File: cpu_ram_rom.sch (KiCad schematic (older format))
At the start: 14 parts, among them U12 74HCT3G04, U4 Z84C0010AEG, U5 IS62C5128BL-45TLI, U6 SST39SF040

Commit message: layout changes, silkscreen fixes
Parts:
- removed D13, D14: Green, LED_SMD:LED_0603_1608Metric_Pad1.05x0.95mm_HandSolder, symbol Device:LED
- removed R40, R41: 360R, Resistor_SMD:R_0603_1608Metric_Pad1.05x0.95mm_HandSolder, symbol Device:R_Small
- removed U12: 74HCT3G04, Package_SO:TSSOP-8_3x3mm_P0.65mm, symbol THS-80-rescue:74HCT3G04-74xGxx
- added D2, D3: GRN, LED_SMD:LED_0603_1608Metric_Pad1.05x0.95mm_HandSolder, symbol Device:LED
- added D4: RED, LED_SMD:LED_0603_1608Metric_Pad1.05x0.95mm_HandSolder, symbol Device:LED
- added R10, R11: 1K, Resistor_SMD:R_0603_1608Metric_Pad1.05x0.95mm_HandSolder, symbol Device:R_Small
- added R12: 360R, Resistor_SMD:R_0603_1608Metric_Pad1.05x0.95mm_HandSolder, symbol Device:R_Small
- added U5: 74LVC2G02, Package_SO:TSSOP-8_3x3mm_P0.65mm, symbol 74xGxx:74LVC2G02
- renumbered C18 to C10, C16 to C8, C17 to C9, R19 to R7, R21 to R8, R20 to R9, U5 to U3, U6 to U4, U4 to U6
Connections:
- net labels added: VCC
- net labels removed: +5V
- wire segments 117 -> 118
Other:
- note added: "RAM Enabled"
- note added: "ROM Enabled"
- note added: "ROM Write Enabled"

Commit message: started routing
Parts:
- removed U3: IS62C5128BL-45TLI, Package_SO:TSOP-II-32_21.0x10.2mm_P1.27mm, symbol THS-80:IS62C5128BL-45TLI
- added U3: AS6C4008A-55ZIN, Package_SO:TSOP-II-32_21.0x10.2mm_P1.27mm, symbol Memory_RAM:AS6C4008A-55ZIN
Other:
- moved on the sheet: R7, R8, R9, U4

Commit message: changes
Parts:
- U3: symbol Memory_RAM:AS6C4008A-55ZIN -> THS-80-rescue:AS6C4008A-55ZIN-Memory_RAM
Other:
- moved on the sheet: U6

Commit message: cleaned up
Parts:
- removed U5: 74LVC2G02, Package_SO:TSSOP-8_3x3mm_P0.65mm, symbol 74xGxx:74LVC2G02
- added U14: 74AHCT2G04, Package_TO_SOT_SMD:SOT-363_SC-70-6_Handsoldering, symbol 74xGxx:74LVC2G04
- added U5: 74AHCT1G02, Package_TO_SOT_SMD:SOT-353_SC-70-5_Handsoldering, symbol 74xGxx:74AHCT1G02
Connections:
- wire segments 118 -> 115
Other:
- moved on the sheet: C10, C8, C9, D3, D4, R11, R12

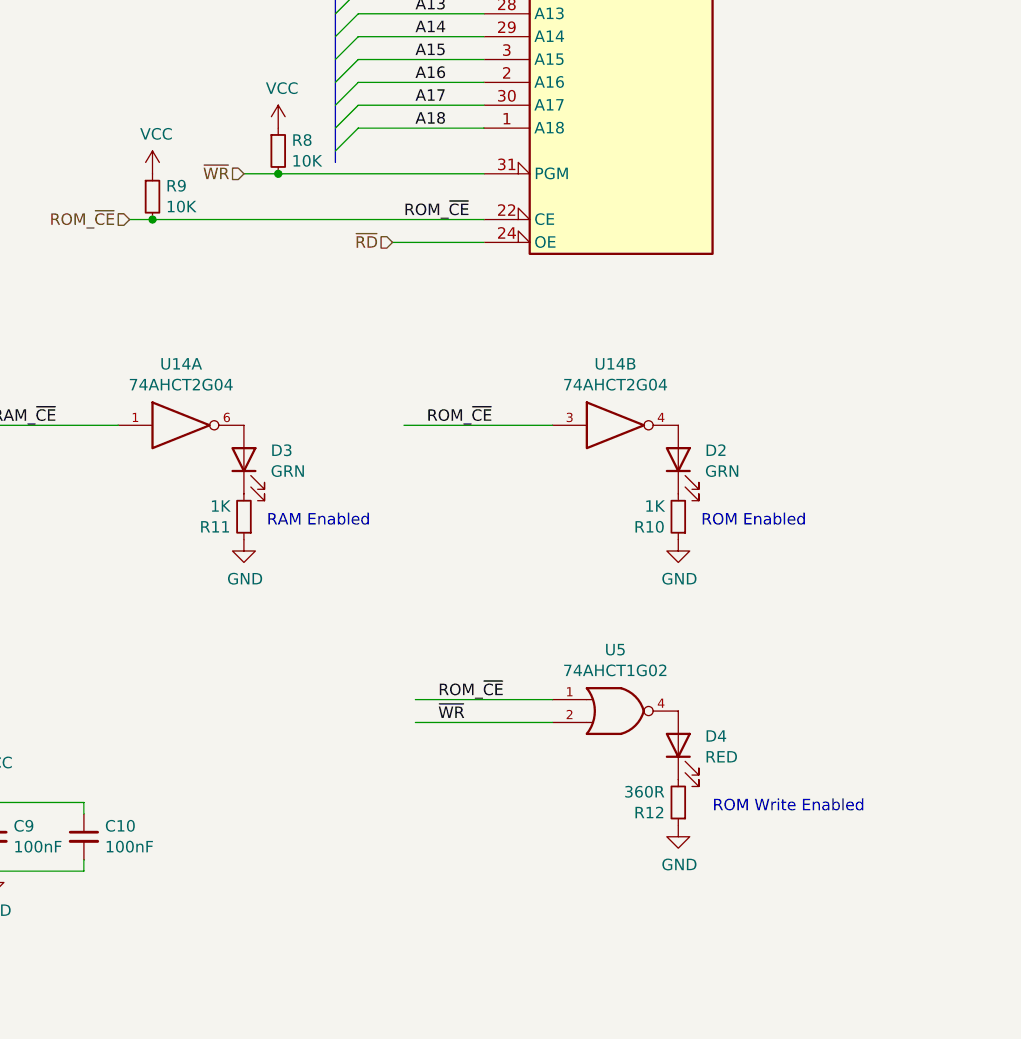
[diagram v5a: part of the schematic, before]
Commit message: Fixes for rom
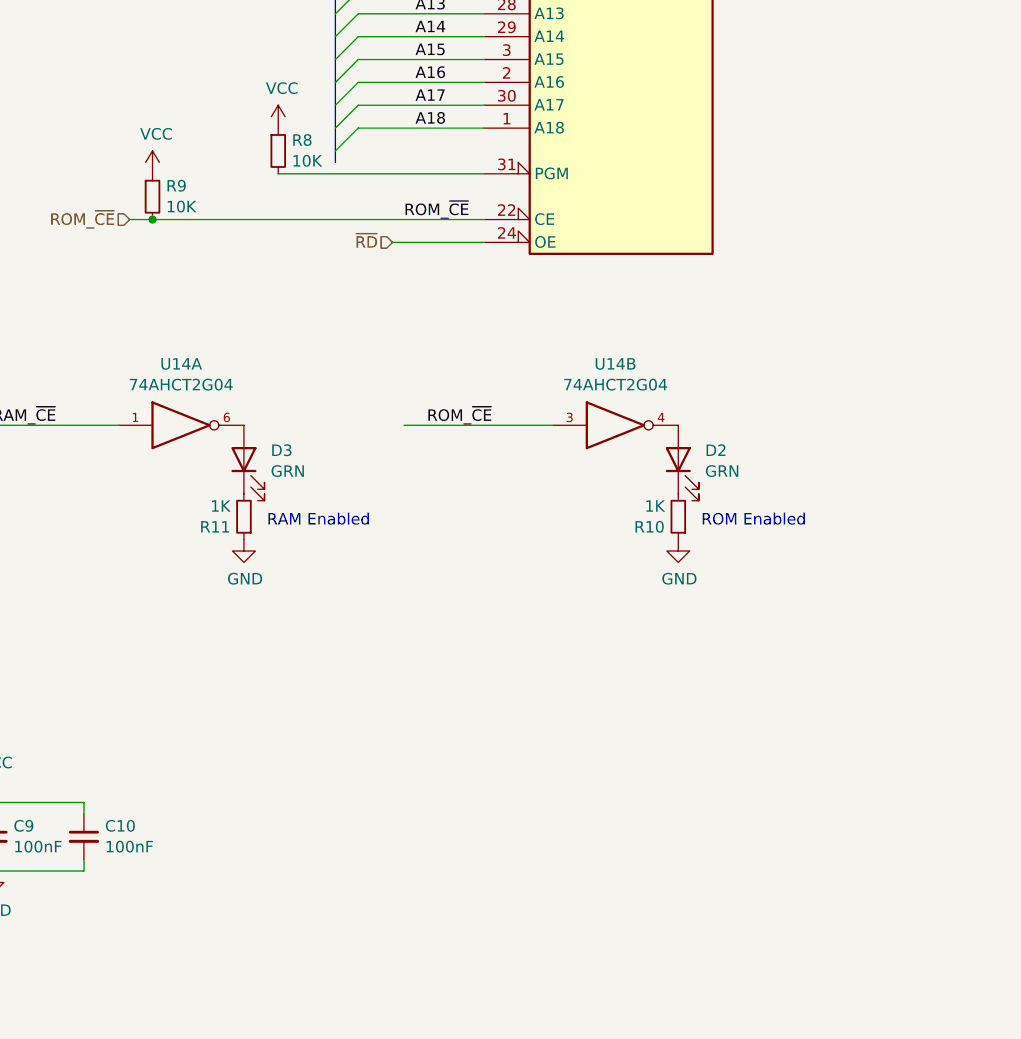
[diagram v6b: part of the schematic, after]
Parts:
- removed D4: RED, LED_SMD:LED_0603_1608Metric_Pad1.05x0.95mm_HandSolder, symbol Device:LED
- removed R12: 360R, Resistor_SMD:R_0603_1608Metric_Pad1.05x0.95mm_HandSolder, symbol Device:R_Small
- removed U5: 74AHCT1G02, Package_TO_SOT_SMD:SOT-353_SC-70-5_Handsoldering, symbol 74xGxx:74AHCT1G02
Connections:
- net ~WR: no longer R8.2, U4.31 (PGM)
- new net: R8.2, U4.31 (PGM)
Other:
- note removed: "ROM Write Enabled"
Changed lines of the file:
@@
 EESchema Schematic File Version 4
-LIBS:THS-80-cache
 EELAYER 30 0
 EELAYER END
@@
 Text HLabel 10850 1200 2    50   3State ~ 0
 D[0..7]
-Text HLabel 7950 2800 0    50   Input ~ 0
-~WR
-Connection ~ 8100 2800
-Wire Wire Line
-	8100 2800 7950 2800
 Text Label 8650 3000 0    50   ~ 0
 ROM_~CE
@@
 	-1   0    0    1
 $EndComp
-$Comp
-L power:GND #PWR026
-U 1 1 5DA13CEA
-P 9850 5650
-F 0 "#PWR026" H 9850 5400 50  0001 C CNN
-F 1 "GND" H 9855 5477 50  0000 C CNN
-F 2 "" H 9850 5650 50  0001 C CNN
-F 3 "" H 9850 5650 50  0001 C CNN
-	1    9850 5650
-	1    0    0    -1
-$EndComp
-$Comp
-L Device:LED D4
-U 1 1 5DA13CF0
-P 9850 5300
-F 0 "D4" V 9889 5183 50  0000 R CNN
-F 1 "RED" V 9798 5183 50  0000 R CNN
-F 2 "LED_SMD:LED_0603_1608Metric_Pad1.05x0.95mm_HandSolder" H 9850 5300 50  0001 C CNN
-F 3 "~" H 9850 5300 50  0001 C CNN
-	1    9850 5300
-	0    -1   -1   0
-$EndComp
-$Comp
-L Device:R_Small R12
-U 1 1 5DA13CF6
-P 9850 5550
-F 0 "R12" H 9909 5596 50  0000 L CNN
-F 1 "360R" H 9909 5505 50  0000 L CNN
-F 2 "Resistor_SMD:R_0603_1608Metric_Pad1.05x0.95mm_HandSolder" H 9850 5550 50  0001 C CNN
-F 3 "~" H 9850 5550 50  0001 C CNN
-	1    9850 5550
-	-1   0    0    1
-$EndComp
 Text Notes 8050 4350 0    50   ~ 0
 RAM Enabled
-Text Notes 10000 5600 0    50   ~ 0
-ROM Write Enabled
-Wire Wire Line
-	9300 5100 8700 5100
-Text Label 8800 5100 0    50   ~ 0
-ROM_~CE
-Text Label 8800 5200 0    50   ~ 0
-~WR
-Wire Wire Line
-	9300 5200 8700 5200
 Wire Wire Line
 	7400 3900 6750 3900
@@
 	1    0    0    -1
 $EndComp
-$Comp
-L 74xGxx:74AHCT1G02 U5
-U 1 1 5DC6BE1B
-P 9600 5150
-F 0 "U5" H 9575 5417 50  0000 C CNN
-F 1 "74AHCT1G02" H 9575 5326 50  0000 C CNN
-F 2 "Package_TO_SOT_SMD:SOT-353_SC-70-5_Handsoldering" H 9600 5150 50  0001 C CNN
-F 3 "http://www.ti.com/lit/sg/scyt129e/scyt129e.pdf" H 9600 5150 50  0001 C CNN
-	1    9600 5150
-	1    0    0    -1
-$EndComp

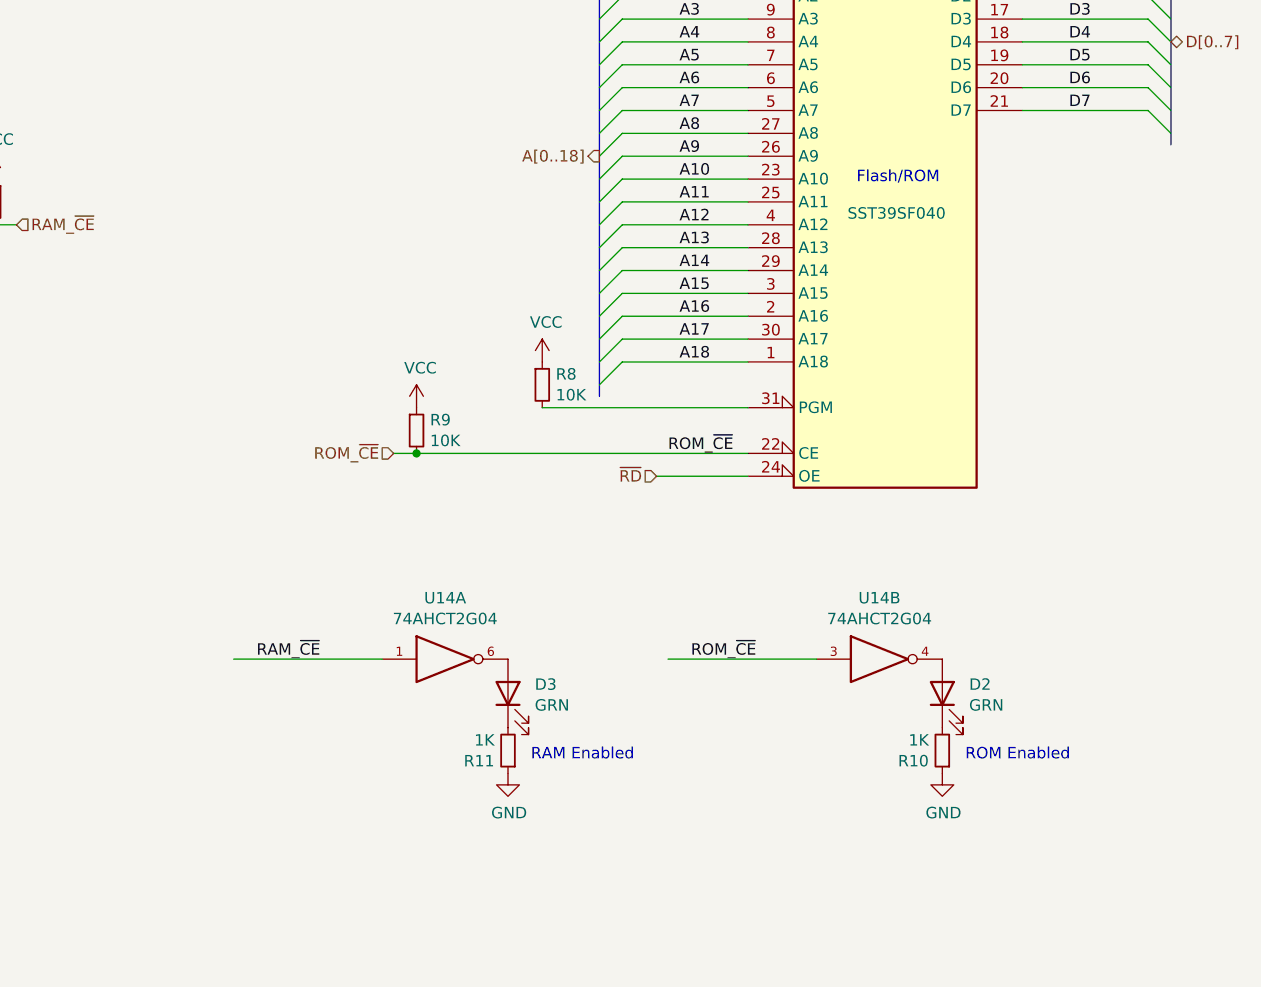
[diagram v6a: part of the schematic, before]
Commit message: Added reset and rom write ena jumpers
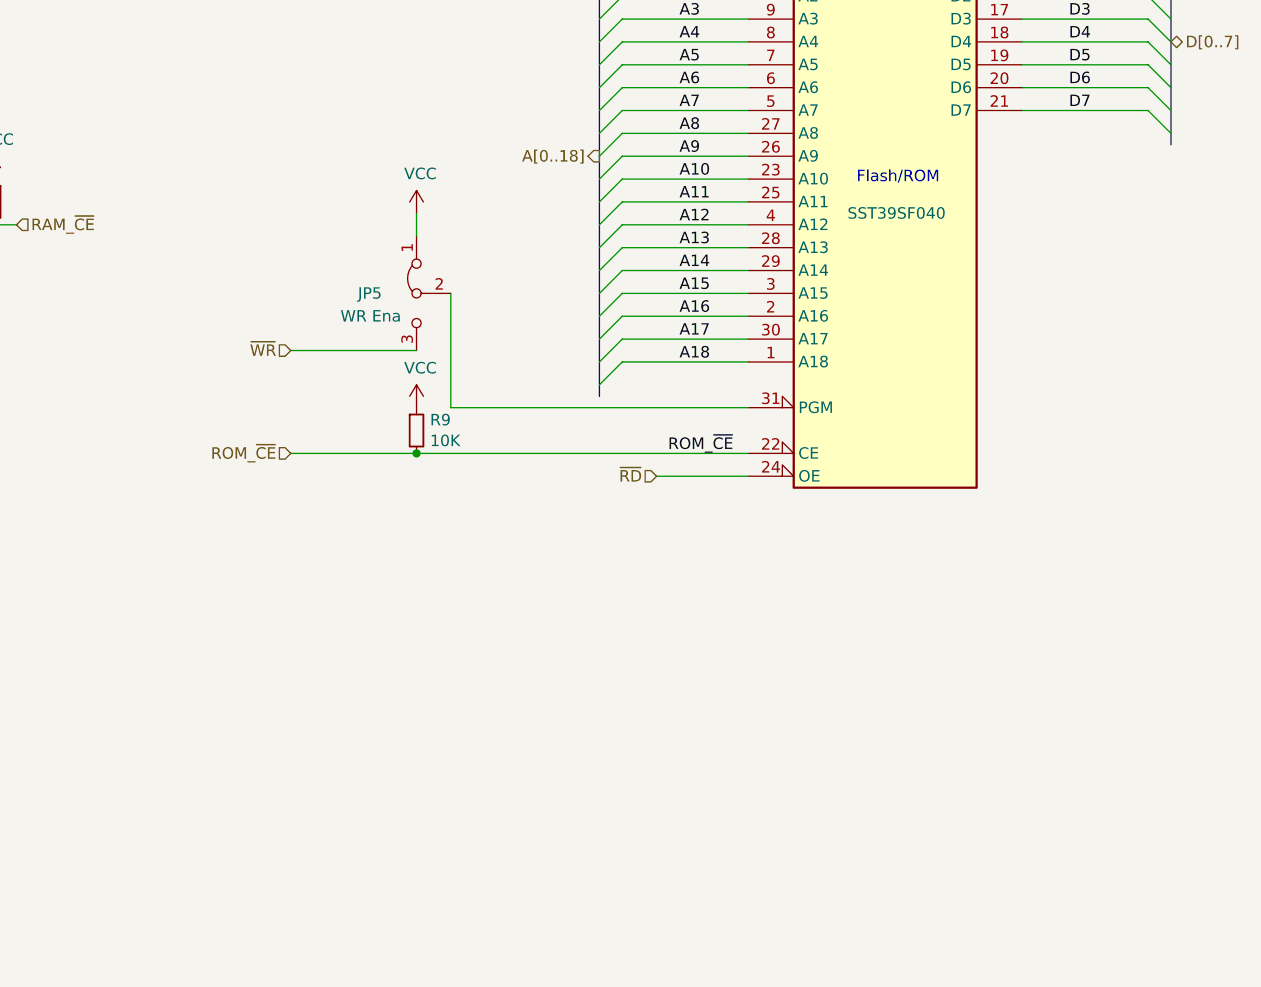
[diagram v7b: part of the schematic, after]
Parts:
- removed D2, D3: GRN, LED_SMD:LED_0603_1608Metric_Pad1.05x0.95mm_HandSolder, symbol Device:LED
- removed R10, R11: 1K, Resistor_SMD:R_0603_1608Metric_Pad1.05x0.95mm_HandSolder, symbol Device:R_Small
- removed R8: 10K, Resistor_SMD:R_0603_1608Metric_Pad1.05x0.95mm_HandSolder, symbol Device:R_Small
- removed U14: 74AHCT2G04, Package_TO_SOT_SMD:SOT-363_SC-70-6_Handsoldering, symbol 74xGxx:74LVC2G04
- added JP5: WR Ena, Connector_PinHeader_2.54mm:PinHeader_1x03_P2.54mm_Vertical, symbol Jumper:Jumper_3_Bridged12
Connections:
- net VCC: now also JP5.1 (A)
- net ~WR: now also JP5.3 (B)
- net at U4.31 (PGM): now also JP5.2 (C)
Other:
- note removed: "RAM Enabled"
- note removed: "ROM Enabled"
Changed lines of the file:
@@
 ~RD
-Wire Wire Line
-	8100 2800 9000 2800
 Wire Wire Line
 	8450 2500 9000 2500
@@
 Wire Wire Line
 	10200 800  10750 800
-Text HLabel 7450 3000 0    50   Input ~ 0
+Text HLabel 7000 3000 0    50   Input ~ 0
 ROM_~CE~
 Text Notes 9475 1825 0    50   ~ 0
@@
 Wire Wire Line
 	9000 3100 8600 3100
-$Comp
-L Device:R_Small R8
-U 1 1 5D6532C1
-P 8100 2700
-F 0 "R8" H 8159 2746 50  0000 L CNN
-F 1 "10K" H 8159 2655 50  0000 L CNN
-F 2 "Resistor_SMD:R_0603_1608Metric_Pad1.05x0.95mm_HandSolder" H 8100 2700 50  0001 C CNN
-F 3 "~" H 8100 2700 50  0001 C CNN
-	1    8100 2700
-	1    0    0    -1
-$EndComp
 Connection ~ 5700 2000
 Wire Wire Line
 	5700 2000 5800 2000
 Connection ~ 7550 3000
-Wire Wire Line
-	7550 3000 7450 3000
 $Comp
 L Device:C_Small C8
@@
 Wire Wire Line
 	6850 5850 7250 5850
-$Comp
-L power:GND #PWR025
-U 1 1 5DA13CCB
-P 7950 4400
-F 0 "#PWR025" H 7950 4150 50  0001 C CNN
-F 1 "GND" H 7955 4227 50  0000 C CNN
-F 2 "" H 7950 4400 50  0001 C CNN
-F 3 "" H 7950 4400 50  0001 C CNN
-	1    7950 4400
-	1    0    0    -1
-$EndComp
-Text Label 6850 3900 0    50   ~ 0
-RAM_~CE
-$Comp
-L Device:LED D3
-U 1 1 5DA13CDE
-P 7950 4050
-F 0 "D3" V 7989 3933 50  0000 R CNN
-F 1 "GRN" V 7898 3933 50  0000 R CNN
-F 2 "LED_SMD:LED_0603_1608Metric_Pad1.05x0.95mm_HandSolder" H 7950 4050 50  0001 C CNN
-F 3 "~" H 7950 4050 50  0001 C CNN
-	1    7950 4050
-	0    -1   -1   0
-$EndComp
-$Comp
-L Device:R_Small R11
-U 1 1 5DA13CE4
-P 7950 4300
-F 0 "R11" H 8009 4346 50  0000 L CNN
-F 1 "1K" H 8009 4255 50  0000 L CNN
-F 2 "Resistor_SMD:R_0603_1608Metric_Pad1.05x0.95mm_HandSolder" H 7950 4300 50  0001 C CNN
-F 3 "~" H 7950 4300 50  0001 C CNN
-	1    7950 4300
-	-1   0    0    1
-$EndComp
-Text Notes 8050 4350 0    50   ~ 0
-RAM Enabled
-Wire Wire Line
-	7400 3900 6750 3900
 Wire Wire Line
 	7550 3000 9000 3000
@@
 L power:VCC #PWR?
 U 1 1 5DCA243D
-P 8100 2600
+P 7550 1950
 AR Path="/5DCA243D" Ref="#PWR?"  Part="1"
 AR Path="/5D6224DC/5DCA243D" Ref="#PWR0107"  Part="1"
-F 0 "#PWR0107" H 8100 2450 50  0001 C CNN
-F 1 "VCC" H 8117 2773 50  0000 C CNN
-F 2 "" H 8100 2600 50  0001 C CNN
-F 3 "" H 8100 2600 50  0001 C CNN
-	1    8100 2600
+F 0 "#PWR0107" H 7550 1800 50  0001 C CNN
+F 1 "VCC" H 7567 2123 50  0000 C CNN
+F 2 "" H 7550 1950 50  0001 C CNN
+F 3 "" H 7550 1950 50  0001 C CNN
+	1    7550 1950
 	1    0    0    -1
 $EndComp
@@
 $EndComp
 $Comp
-L power:GND #PWR01
-U 1 1 5DBEF08F
-P 9850 4400
-F 0 "#PWR01" H 9850 4150 50  0001 C CNN
-F 1 "GND" H 9855 4227 50  0000 C CNN
-F 2 "" H 9850 4400 50  0001 C CNN
-F 3 "" H 9850 4400 50  0001 C CNN
-	1    9850 4400
-	1    0    0    -1
-$EndComp
-Text Label 8750 3900 0    50   ~ 0
-ROM_~CE
-$Comp
-L Device:LED D2
-U 1 1 5DBEF096
-P 9850 4050
-F 0 "D2" V 9889 3933 50  0000 R CNN
-F 1 "GRN" V 9798 3933 50  0000 R CNN
-F 2 "LED_SMD:LED_0603_1608Metric_Pad1.05x0.95mm_HandSolder" H 9850 4050 50  0001 C CNN
-F 3 "~" H 9850 4050 50  0001 C CNN
-	1    9850 4050
-	0    -1   -1   0
-$EndComp
-$Comp
-L Device:R_Small R10
-U 1 1 5DBEF09C
-P 9850 4300
-F 0 "R10" H 9909 4346 50  0000 L CNN
-F 1 "1K" H 9909 4255 50  0000 L CNN
-F 2 "Resistor_SMD:R_0603_1608Metric_Pad1.05x0.95mm_HandSolder" H 9850 4300 50  0001 C CNN
-F 3 "~" H 9850 4300 50  0001 C CNN
-	1    9850 4300
-	-1   0    0    1
-$EndComp
-Text Notes 9950 4350 0    50   ~ 0
-ROM Enabled
-Wire Wire Line
-	9300 3900 8650 3900
-$Comp
-L 74xGxx:74LVC2G04 U14
-U 1 1 5DBF5BBF
-P 7700 3900
-F 0 "U14" H 7675 4167 50  0000 C CNN
-F 1 "74AHCT2G04" H 7675 4076 50  0000 C CNN
-F 2 "Package_TO_SOT_SMD:SOT-363_SC-70-6_Handsoldering" H 7700 3900 50  0001 C CNN
-F 3 "http://www.ti.com/lit/sg/scyt129e/scyt129e.pdf" H 7700 3900 50  0001 C CNN
-	1    7700 3900
-	1    0    0    -1
-$EndComp
-$Comp
-L 74xGxx:74LVC2G04 U14
-U 2 1 5DBF69CE
-P 9600 3900
-F 0 "U14" H 9575 4167 50  0000 C CNN
-F 1 "74AHCT2G04" H 9575 4076 50  0000 C CNN
-F 2 "Package_TO_SOT_SMD:SOT-363_SC-70-6_Handsoldering" H 9600 3900 50  0001 C CNN
-F 3 "http://www.ti.com/lit/sg/scyt129e/scyt129e.pdf" H 9600 3900 50  0001 C CNN
-	2    9600 3900
-	1    0    0    -1
-$EndComp
+L Jumper:Jumper_3_Bridged12 JP?
+U 1 1 5EA41998
+P 7550 2300
+AR Path="/5EA41998" Ref="JP?"  Part="1"
+AR Path="/5D6224DC/5EA41998" Ref="JP5"  Part="1"
+F 0 "JP5" V 7550 2504 50  0000 C CNN
+F 1 "WR Ena" V 7650 2500 50  0000 C CNN
+F 2 "Connector_PinHeader_2.54mm:PinHeader_1x03_P2.54mm_Vertical" H 7550 2300 50  0001 C CNN
+F 3 "~" H 7550 2300 50  0001 C CNN
+	1    7550 2300
+	0    -1   1    0
+$EndComp
+Wire Wire Line
+	7550 2550 7000 2550
+Text HLabel 7000 2550 0    50   Input ~ 0
+~WR
+Wire Wire Line
+	7550 1950 7550 2050
+Wire Wire Line
+	9000 2800 7700 2800
+Wire Wire Line
+	7700 2800 7700 2300
+Wire Wire Line
+	7000 3000 7550 3000
 Wire Bus Line
 	10850 850  10850 1650

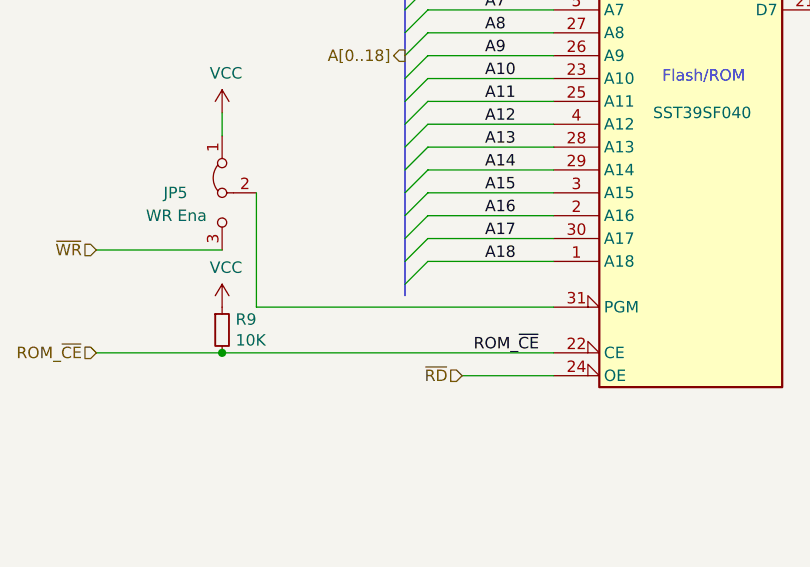
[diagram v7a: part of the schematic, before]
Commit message: Changed to resistor arrays, flipped to front-side
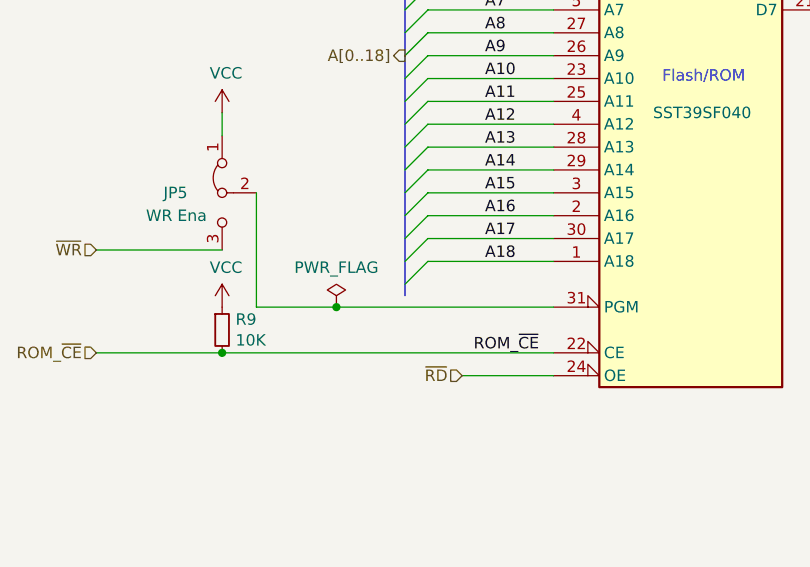
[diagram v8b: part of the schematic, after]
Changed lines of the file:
@@
 	7550 1950 7550 2050
 Wire Wire Line
-	9000 2800 7700 2800
+	9000 2800 8050 2800
 Wire Wire Line
 	7700 2800 7700 2300
 Wire Wire Line
 	7000 3000 7550 3000
+$Comp
+L power:PWR_FLAG #FLG02
+U 1 1 5E91C5ED
+P 8050 2800
+F 0 "#FLG02" H 8050 2875 50  0001 C CNN
+F 1 "PWR_FLAG" H 8050 2973 50  0000 C CNN
+F 2 "" H 8050 2800 50  0001 C CNN
+F 3 "~" H 8050 2800 50  0001 C CNN
+	1    8050 2800
+	1    0    0    -1
+$EndComp
+Connection ~ 8050 2800
+Wire Wire Line
+	8050 2800 7700 2800
 Wire Bus Line
 	10850 850  10850 1650
